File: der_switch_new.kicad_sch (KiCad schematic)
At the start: 8 parts

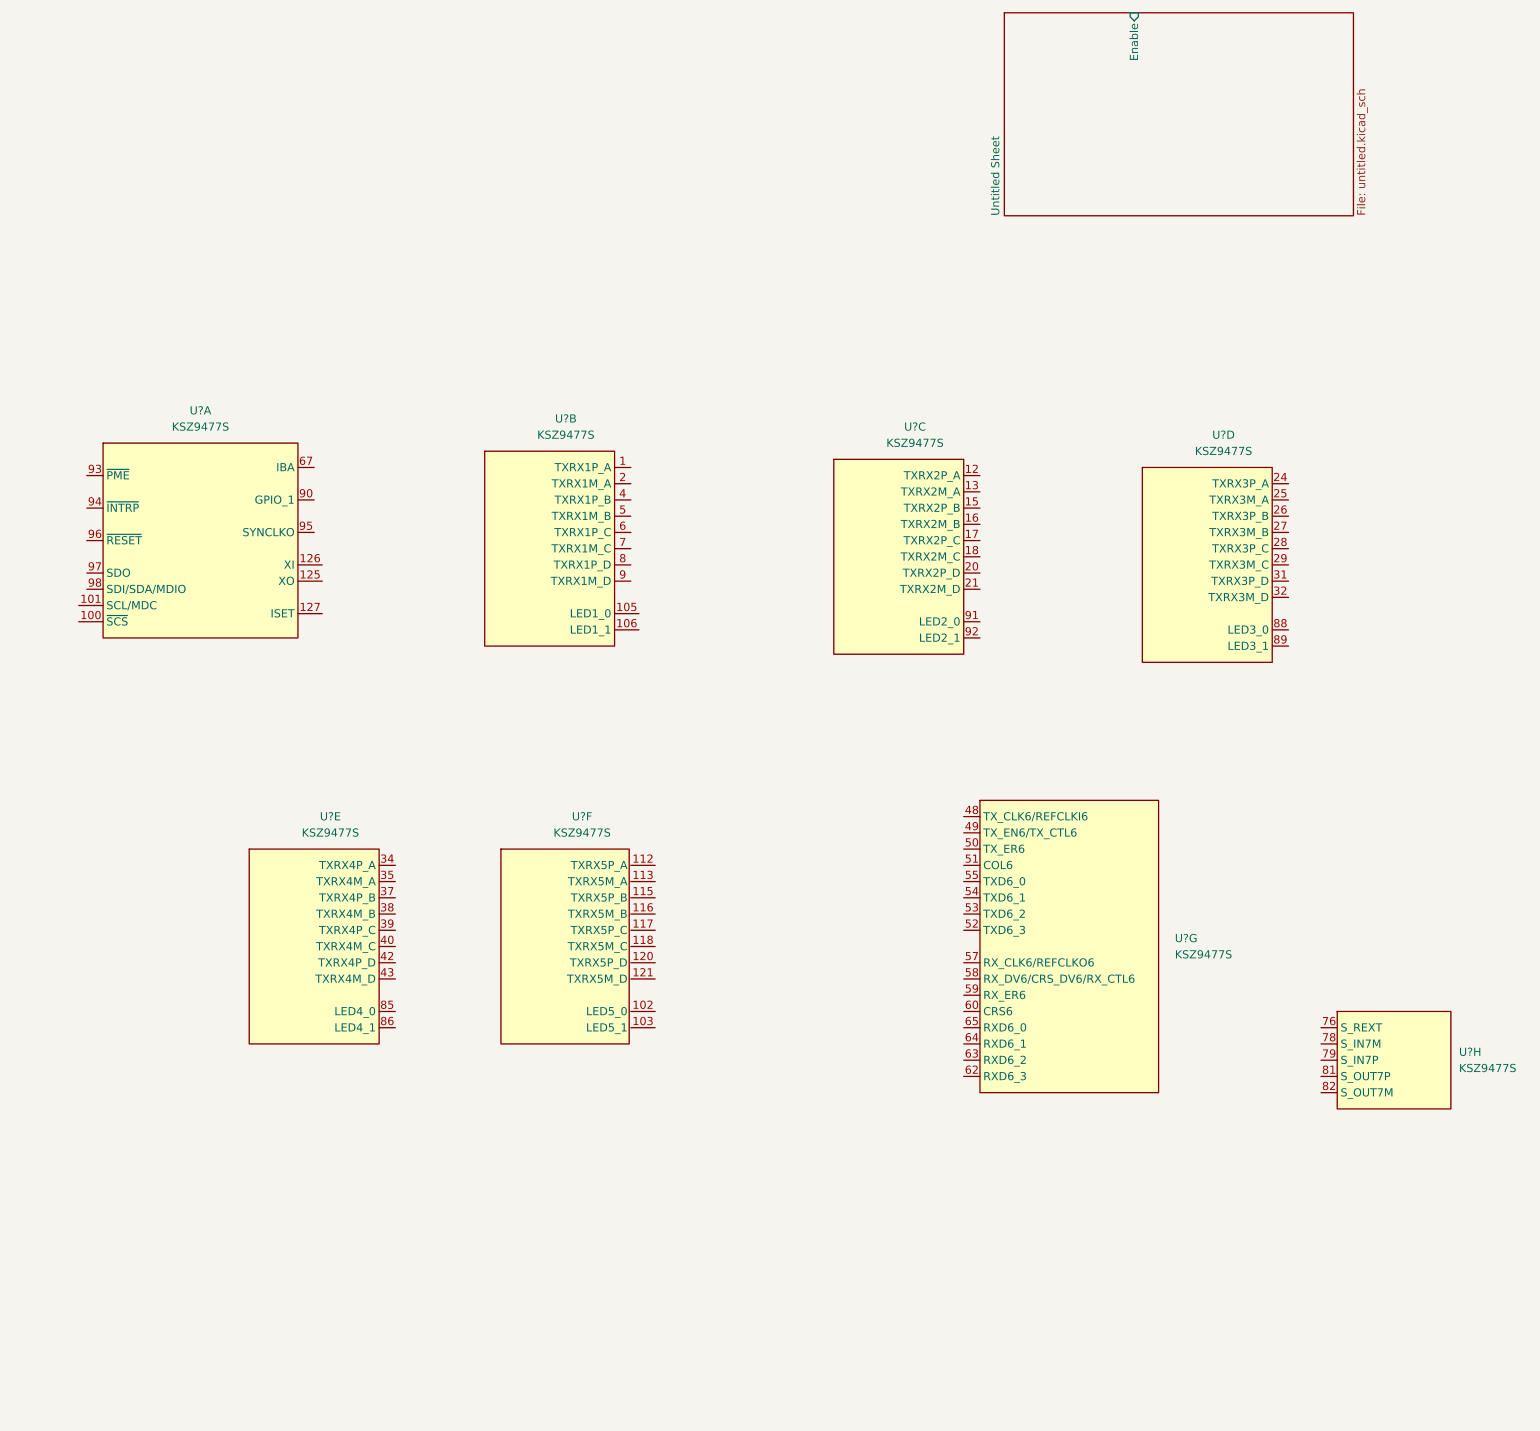
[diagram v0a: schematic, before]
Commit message: Add power supply to the KSZ9477S
Signed-off-by: Oleksij Rempel <linux@rempel-privat.de>
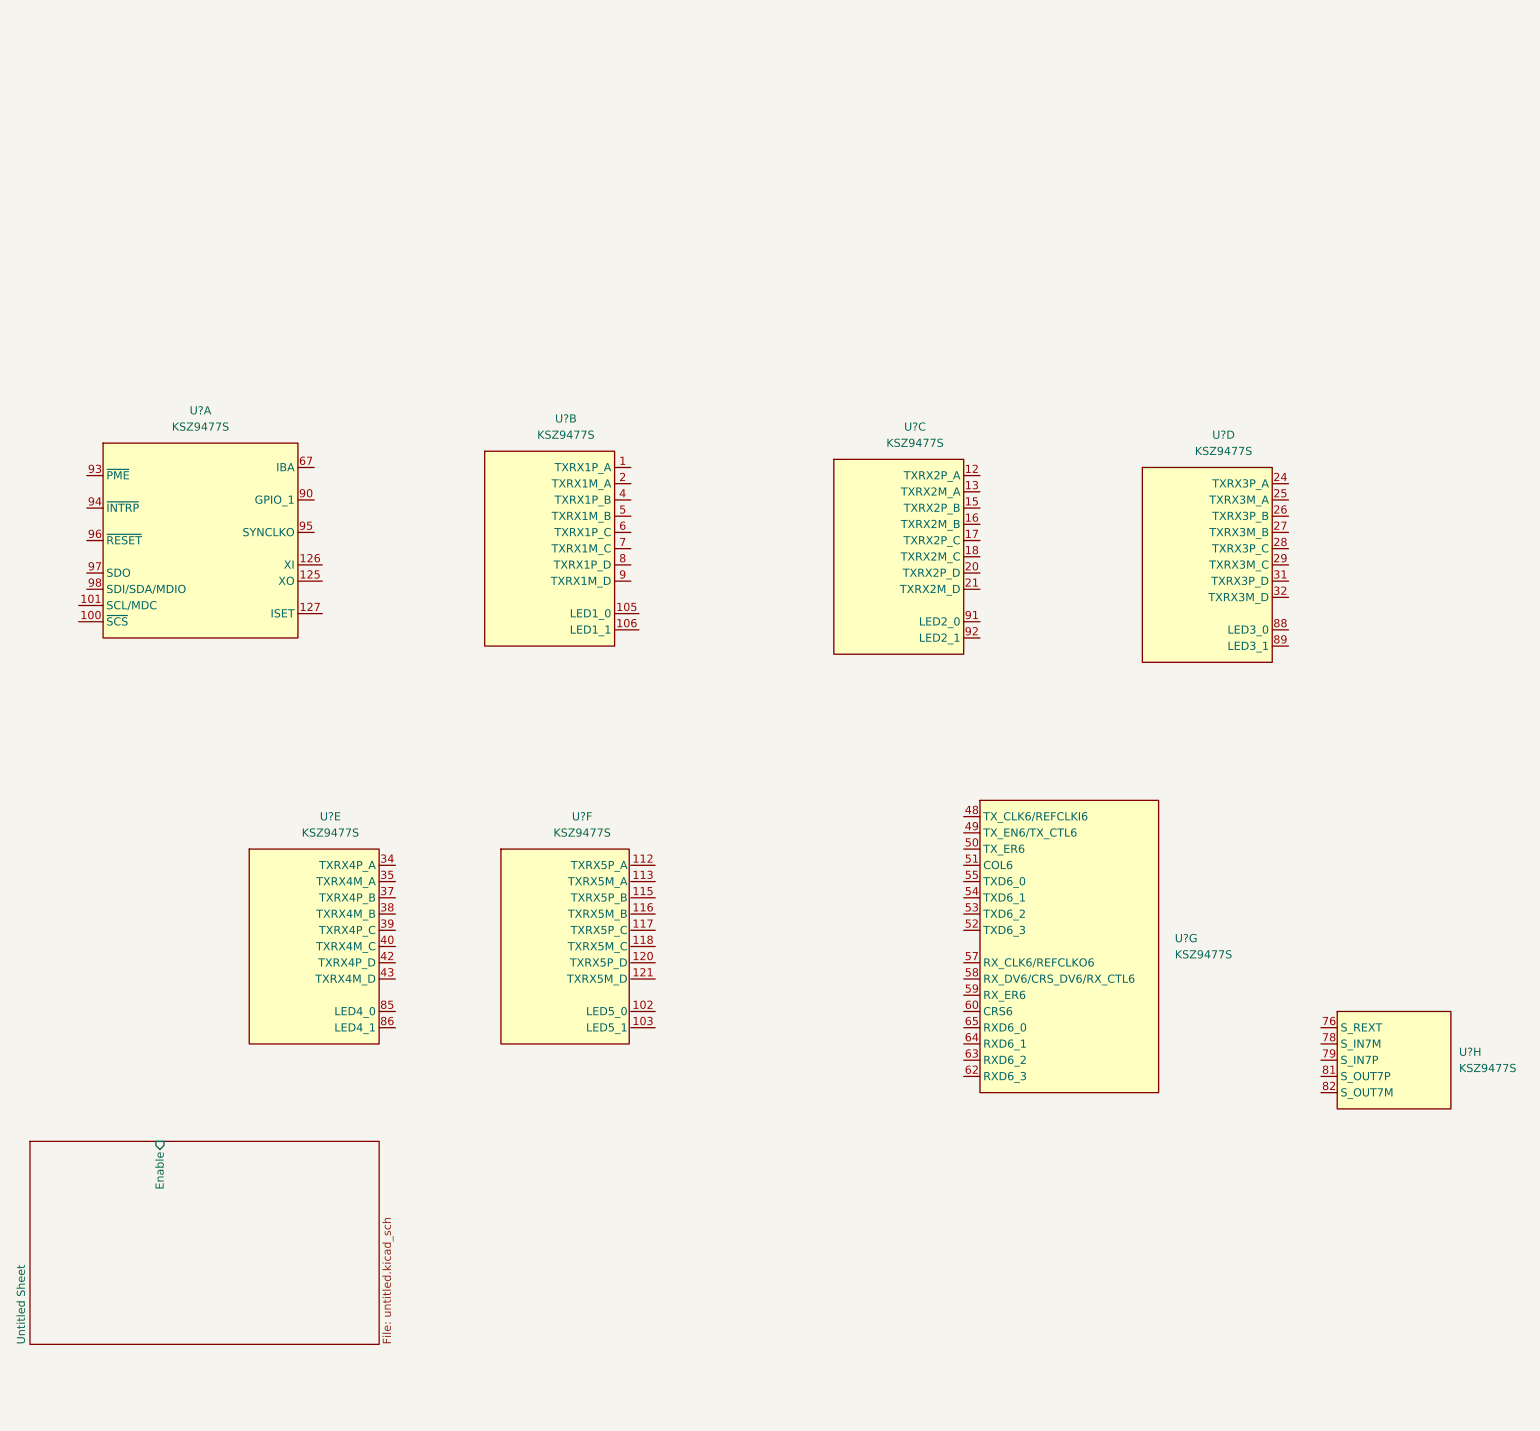
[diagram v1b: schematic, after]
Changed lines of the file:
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@@
     )
   )
-  (sheet (at 187.96 -40.64) (size 54.61 31.75)
+  (sheet (at 35.56 135.89) (size 54.61 31.75)
     (stroke (width 0.001) (type solid) (color 132 0 132 1))
     (fill (color 255 255 255 0.0000))
-    (property "Schaltplanname" "Untitled Sheet" (id 0) (at 187.3241 -8.89 90)
+    (property "Schaltplanname" "Untitled Sheet" (id 0) (at 34.9241 167.64 90)
       (effects (font (size 1.27 1.27)) (justify left bottom))
     )
-    (property "Sheet file" "untitled.kicad_sch" (id 1) (at 243.0789 -8.89 90)
+    (property "Sheet file" "untitled.kicad_sch" (id 1) (at 90.6789 167.64 90)
       (effects (font (size 1.27 1.27)) (justify left top))
     )
-    (pin "Enable" input (at 208.28 -40.64 90)
+    (pin "Enable" input (at 55.88 135.89 90)
       (effects (font (size 1.27 1.27)) (justify right))
     )
@@
       (reference "U?") (unit 8) (value "KSZ9477S") (footprint "Package_QFP:TQFP-128_14x14mm_P0.4mm")
     )
+    (path "/71aecc81-5a5e-4293-ac09-31c20a082000/49f6e3c7-ae3e-4f04-be36-fdc79ed9ee88"
+      (reference "#PWR?") (unit 1) (value "GND") (footprint "")
+    )
+    (path "/71aecc81-5a5e-4293-ac09-31c20a082000/51a0b03e-3923-4cc7-8d85-300208e87472"
+      (reference "#PWR?") (unit 1) (value "+1V2") (footprint "")
+    )
+    (path "/71aecc81-5a5e-4293-ac09-31c20a082000/536ca4d7-317a-460c-97da-cb86d74c7c81"
+      (reference "#PWR?") (unit 1) (value "GND") (footprint "")
+    )
+    (path "/71aecc81-5a5e-4293-ac09-31c20a082000/64182846-cada-49dd-8527-6959da40f69f"
+      (reference "#PWR?") (unit 1) (value "+1V2") (footprint "")
+    )
+    (path "/71aecc81-5a5e-4293-ac09-31c20a082000/70c6fc00-a988-46fb-8f90-ff92a86db5fd"
+      (reference "#PWR?") (unit 1) (value "+3V3") (footprint "")
+    )
+    (path "/71aecc81-5a5e-4293-ac09-31c20a082000/825fa46c-c2e6-4507-b266-35ce5494983a"
+      (reference "#PWR?") (unit 1) (value "GND") (footprint "")
+    )
+    (path "/71aecc81-5a5e-4293-ac09-31c20a082000/84c394c6-a60e-4810-9215-d9cb774f8078"
+      (reference "#PWR?") (unit 1) (value "+2V5") (footprint "")
+    )
+    (path "/71aecc81-5a5e-4293-ac09-31c20a082000/9e70ea58-3902-4564-bb96-3c390b0148ad"
+      (reference "#PWR?") (unit 1) (value "GND") (footprint "")
+    )
+    (path "/71aecc81-5a5e-4293-ac09-31c20a082000/ac68cf9b-7545-4f62-aa4a-7fbaf7998e3a"
+      (reference "#PWR?") (unit 1) (value "+2V5") (footprint "")
+    )
+    (path "/71aecc81-5a5e-4293-ac09-31c20a082000/cda32680-ceab-42d8-97a6-62c28e48eb9d"
+      (reference "#PWR?") (unit 1) (value "GND") (footprint "")
+    )
+    (path "/71aecc81-5a5e-4293-ac09-31c20a082000/d97372bb-f368-4523-a40a-db92458fe7c8"
+      (reference "#PWR?") (unit 1) (value "GND") (footprint "")
+    )
     (path "/71aecc81-5a5e-4293-ac09-31c20a082000/e6d4a224-4104-4eee-8813-491d537eeb18"
       (reference "#PWR?") (unit 1) (value "GND") (footprint "")
     )
+    (path "/71aecc81-5a5e-4293-ac09-31c20a082000/efdfbac8-4180-4ed8-8662-022635dfd59d"
+      (reference "#PWR?") (unit 1) (value "+1V2") (footprint "")
+    )
+    (path "/71aecc81-5a5e-4293-ac09-31c20a082000/029c19dc-5f44-4900-9d54-5b1e56107a18"
+      (reference "C?") (unit 1) (value "0.1 uF") (footprint "")
+    )
+    (path "/71aecc81-5a5e-4293-ac09-31c20a082000/054b1a4a-5bf3-4727-9f60-9104c8fd32ee"
+      (reference "C?") (unit 1) (value "0.1 uF") (footprint "")
+    )
+    (path "/71aecc81-5a5e-4293-ac09-31c20a082000/0847b511-b4b3-4920-b0f3-86e31bb58d77"
+      (reference "C?") (unit 1) (value "0.1 uF") (footprint "")
+    )
+    (path "/71aecc81-5a5e-4293-ac09-31c20a082000/0951ae48-2c5b-4441-8850-2a77f033f014"
+      (reference "C?") (unit 1) (value "0.1 uF") (footprint "")
+    )
+    (path "/71aecc81-5a5e-4293-ac09-31c20a082000/0e0d658f-df7a-4706-abab-18e4996228b4"
+      (reference "C?") (unit 1) (value "0.1 uF") (footprint "")
+    )
+    (path "/71aecc81-5a5e-4293-ac09-31c20a082000/0ec5692f-6dfd-4474-bbc0-9c70304d38a2"
+      (reference "C?") (unit 1) (value "0.1 uF") (footprint "")
+    )
+    (path "/71aecc81-5a5e-4293-ac09-31c20a082000/18f7a462-ae49-4468-9de6-942a89a60cc0"
+      (reference "C?") (unit 1) (value "22 uF") (footprint "")
+    )
+    (path "/71aecc81-5a5e-4293-ac09-31c20a082000/22fd8967-8edf-4e9e-821e-b19cfb6c94ee"
+      (reference "C?") (unit 1) (value "0.1 uF") (footprint "")
+    )
+    (path "/71aecc81-5a5e-4293-ac09-31c20a082000/257656c1-bb8b-4752-997a-1dd215aac8e9"
+      (reference "C?") (unit 1) (value "22 uF") (footprint "")
+    )
+    (path "/71aecc81-5a5e-4293-ac09-31c20a082000/260ffc39-40a8-439c-ba1f-21e59fd79102"
+      (reference "C?") (unit 1) (value "0.1 uF") (footprint "")
+    )
+    (path "/71aecc81-5a5e-4293-ac09-31c20a082000/34855025-3e26-434f-8b1a-067c64052a88"
+      (reference "C?") (unit 1) (value "0.1 uF") (footprint "")
+    )
+    (path "/71aecc81-5a5e-4293-ac09-31c20a082000/3619d197-ffc0-4839-8609-8ab7ffddd92f"
+      (reference "C?") (unit 1) (value "0.1 uF") (footprint "")
+    )
+    (path "/71aecc81-5a5e-4293-ac09-31c20a082000/3eade6bb-c108-4a17-ab5d-7748ec6178c6"
+      (reference "C?") (unit 1) (value "0.1 uF") (footprint "")
+    )
+    (path "/71aecc81-5a5e-4293-ac09-31c20a082000/3ef741f0-c5e6-4daa-bd7c-d238dc9d6353"
+      (reference "C?") (unit 1) (value "10 uF") (footprint "")
+    )
+    (path "/71aecc81-5a5e-4293-ac09-31c20a082000/43646c4a-e0ea-4378-a8d7-890f874de6b5"
+      (reference "C?") (unit 1) (value "0.1 uF") (footprint "")
+    )
+    (path "/71aecc81-5a5e-4293-ac09-31c20a082000/56d603a6-97c1-4ffa-8db2-9d270396d111"
+      (reference "C?") (unit 1) (value "0.1 uF") (footprint "")
+    )
+    (path "/71aecc81-5a5e-4293-ac09-31c20a082000/5e21245f-7e02-43df-8112-4d4b8d25cfd0"
+      (reference "C?") (unit 1) (value "0.1 uF") (footprint "")
+    )
+    (path "/71aecc81-5a5e-4293-ac09-31c20a082000/63c718bd-dd13-4a59-bffb-2d593735dce1"
+      (reference "C?") (unit 1) (value "0.1 uF") (footprint "")
+    )
+    (path "/71aecc81-5a5e-4293-ac09-31c20a082000/67715ffd-b211-464a-85dc-b728b32e12bb"
+      (reference "C?") (unit 1) (value "0.1 uF") (footprint "")
+    )
+    (path "/71aecc81-5a5e-4293-ac09-31c20a082000/78e72fea-ed4e-453f-84db-79458ec11d3a"
+      (reference "C?") (unit 1) (value "0.1 uF") (footprint "")
+    )
+    (path "/71aecc81-5a5e-4293-ac09-31c20a082000/7f728bc1-fdee-424f-b7d0-18e9fa1d86f6"
+      (reference "C?") (unit 1) (value "0.1 uF") (footprint "")
+    )
+    (path "/71aecc81-5a5e-4293-ac09-31c20a082000/8b32e348-c311-496e-ad32-8c596f12c114"
+      (reference "C?") (unit 1) (value "0.1 uF") (footprint "")
+    )
+    (path "/71aecc81-5a5e-4293-ac09-31c20a082000/92a4dd59-7d70-4c9f-8ed9-0ed40d042aeb"
+      (reference "C?") (unit 1) (value "0.1 uF") (footprint "")
+    )
+    (path "/71aecc81-5a5e-4293-ac09-31c20a082000/a30e82da-48ba-4424-8770-98f0a641dfe6"
+      (reference "C?") (unit 1) (value "0.1 uF") (footprint "")
+    )
+    (path "/71aecc81-5a5e-4293-ac09-31c20a082000/ac15b2d1-eeb7-43a0-b477-dcb40b8d5c3c"
+      (reference "C?") (unit 1) (value "0.1 uF") (footprint "")
+    )
+    (path "/71aecc81-5a5e-4293-ac09-31c20a082000/b5434f42-f7ed-4e7f-8a1a-d3431eebfdfd"
+      (reference "C?") (unit 1) (value "22 uF") (footprint "")
+    )
+    (path "/71aecc81-5a5e-4293-ac09-31c20a082000/b69c8016-ebc9-45e9-ae9a-dc59293304b4"
+      (reference "C?") (unit 1) (value "0.1 uF") (footprint "")
+    )
+    (path "/71aecc81-5a5e-4293-ac09-31c20a082000/c1ad33e7-9d76-42cb-8af7-1b930100b287"
+      (reference "C?") (unit 1) (value "0.1 uF") (footprint "")
+    )
+    (path "/71aecc81-5a5e-4293-ac09-31c20a082000/c2cb81b8-bc1c-4a07-9fba-0f0cd6632b03"
+      (reference "C?") (unit 1) (value "0.1 uF") (footprint "")
+    )
+    (path "/71aecc81-5a5e-4293-ac09-31c20a082000/c373cdd0-f05a-4d43-84da-fb9878d6f7cb"
+      (reference "C?") (unit 1) (value "0.1 uF") (footprint "")
+    )
+    (path "/71aecc81-5a5e-4293-ac09-31c20a082000/c9d86838-75af-4a1e-86d0-e74ef0edfac9"
+      (reference "C?") (unit 1) (value "0.1 uF") (footprint "")
+    )
+    (path "/71aecc81-5a5e-4293-ac09-31c20a082000/cc8e46b4-afdd-4493-bda3-df64383d12a5"
+      (reference "C?") (unit 1) (value "0.1 uF") (footprint "")
+    )
+    (path "/71aecc81-5a5e-4293-ac09-31c20a082000/daa06ce6-b31f-48ba-9d4b-8f80180c30f2"
+      (reference "C?") (unit 1) (value "0.1 uF") (footprint "")
+    )
+    (path "/71aecc81-5a5e-4293-ac09-31c20a082000/e16f6834-187f-4219-b891-014b9c09802f"
+      (reference "C?") (unit 1) (value "0.1 uF") (footprint "")
+    )
+    (path "/71aecc81-5a5e-4293-ac09-31c20a082000/e2f88790-5aab-405e-8d23-0acbc6be77fc"
+      (reference "C?") (unit 1) (value "0.1 uF") (footprint "")
+    )
+    (path "/71aecc81-5a5e-4293-ac09-31c20a082000/ea7353f9-60b3-4c0b-bd82-99c5661ca29e"
+      (reference "C?") (unit 1) (value "22 uF") (footprint "")
+    )
+    (path "/71aecc81-5a5e-4293-ac09-31c20a082000/f0fe2398-3589-483f-a1f4-56e875d64924"
+      (reference "C?") (unit 1) (value "0.1 uF") (footprint "")
+    )
+    (path "/71aecc81-5a5e-4293-ac09-31c20a082000/f6120ccf-ee2d-449d-8be6-7df1e9e105a2"
+      (reference "C?") (unit 1) (value "22 uF") (footprint "")
+    )
+    (path "/71aecc81-5a5e-4293-ac09-31c20a082000/5e483dad-bae1-46ed-90c5-581bc0ec7971"
+      (reference "L?") (unit 1) (value "L_Ferrite") (footprint "")
+    )
+    (path "/71aecc81-5a5e-4293-ac09-31c20a082000/8577f916-1af1-4d24-af11-49d83073d3b3"
+      (reference "L?") (unit 1) (value "L_Ferrite") (footprint "")
+    )
+    (path "/71aecc81-5a5e-4293-ac09-31c20a082000/86f4f89b-86d7-4ff0-b7f8-2bbddc6a0fcb"
+      (reference "L?") (unit 1) (value "L_Ferrite") (footprint "")
+    )
+    (path "/71aecc81-5a5e-4293-ac09-31c20a082000/e52aac40-81ef-404c-b1d0-504973e33cf5"
+      (reference "L?") (unit 1) (value "L_Ferrite") (footprint "")
+    )
     (path "/71aecc81-5a5e-4293-ac09-31c20a082000/9e4a7f6b-5383-44a7-b0de-9b68ac0e96b4"

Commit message: add ports
Signed-off-by: Oleksij Rempel <linux@rempel-privat.de>
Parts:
- removed U? (x5): KSZ9477S, Package_QFP:TQFP-128_14x14mm_P0.4mm, symbol local:KSZ9477S
- gave numbers to parts that had none: 1
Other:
- added sheet ethernet ports (ethernet_ports.kicad_sch)
- sheet Untitled Sheet ports: added none; removed Enable
